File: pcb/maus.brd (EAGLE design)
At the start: 100 x 100 mm, 84 parts, among them J1 SS-52300-001, Q1 BSS123, Q2 BSS123, Q3 BSS123, Q4 BSS123, Q5 BSS123, Q6 PMN30XPEAHEATSINK, Q7 PMN30XPEAHEATSINK, U1 ESP32-S2-WROOM, U2 CH340C, U4 LP3965EMP-3.3, U5 LSM9DS1TR, U6 LM358DR

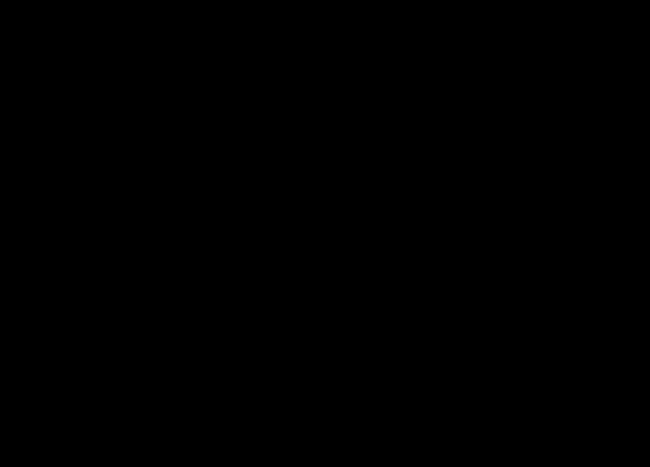
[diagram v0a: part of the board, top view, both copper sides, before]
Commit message: add: lib MBRS360
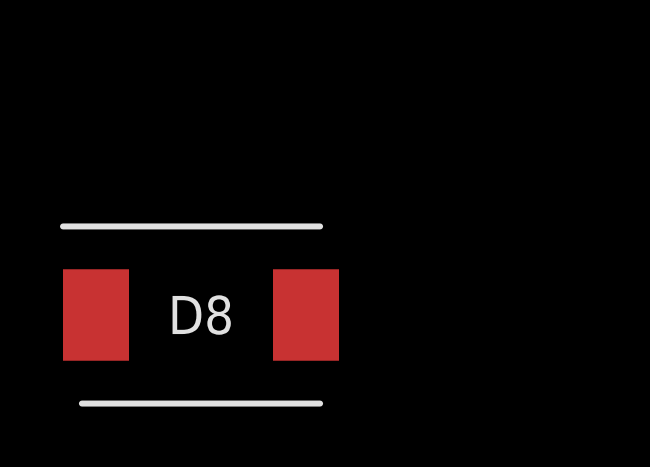
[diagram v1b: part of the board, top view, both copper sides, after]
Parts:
- added D8: VS-MBRS360-M3_9AT, shared:DIOM7959X262N

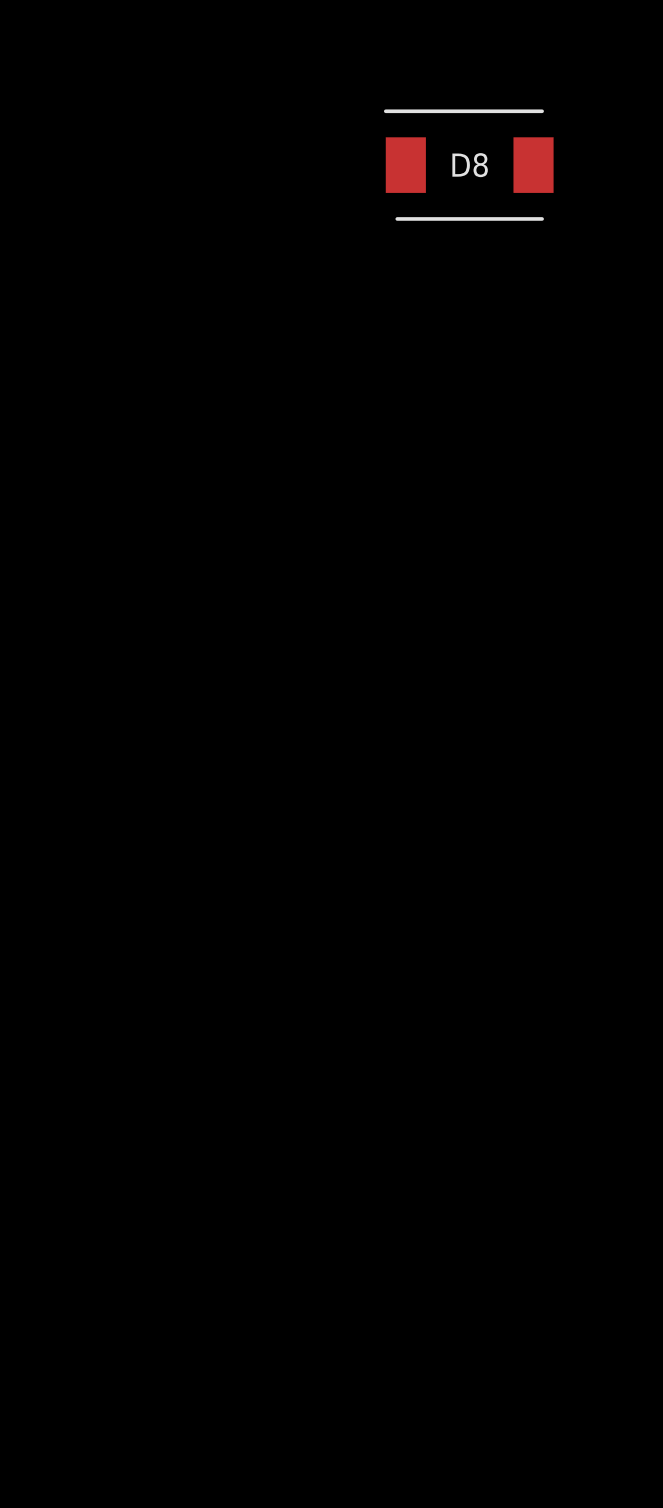
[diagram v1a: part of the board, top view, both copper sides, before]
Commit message: Added diodes for hbridge
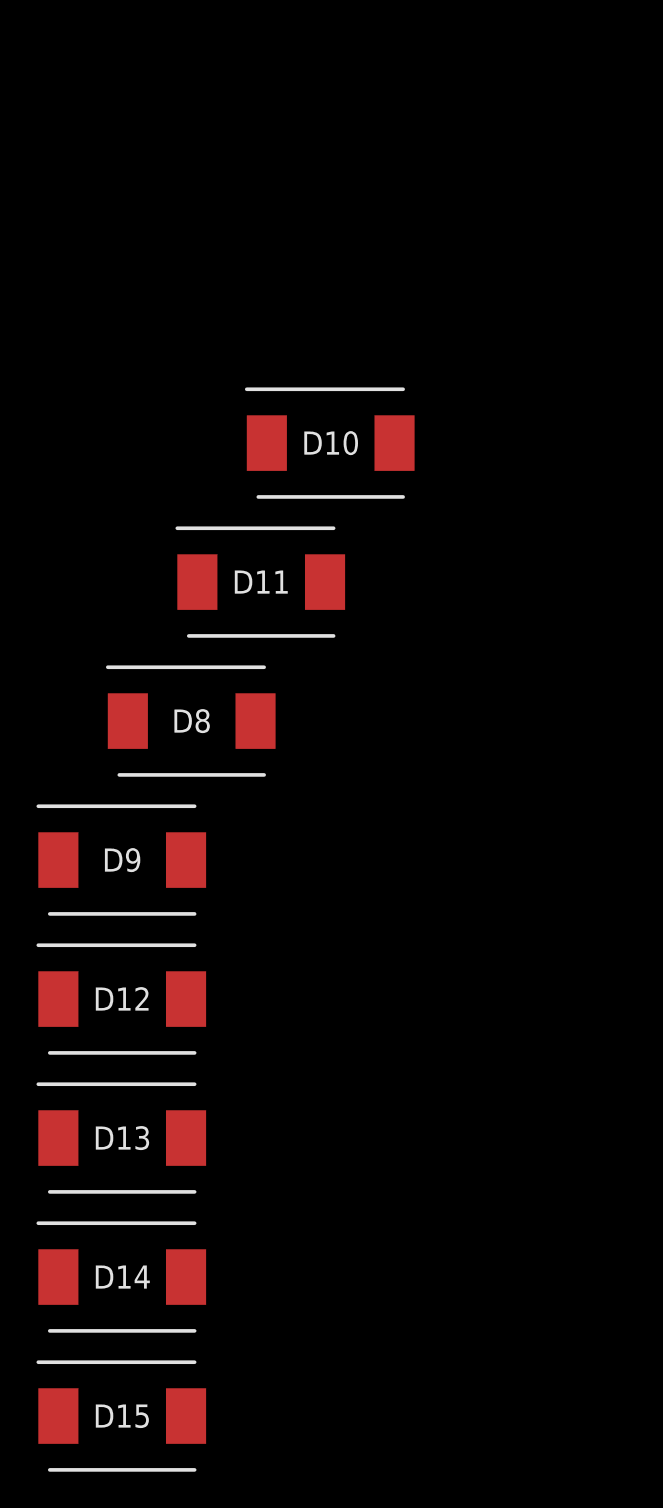
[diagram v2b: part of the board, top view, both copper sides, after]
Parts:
- added D10, D11, D12, D13, D14, D15, D9: VS-MBRS360-M3_9AT, shared:DIOM7959X262N
- moved D8 34.1 mm to (-62.2, -29.2)
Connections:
- net GND: now also D10.2, D11.2, D12.2, D13.2
- net M1_M+: now also D11.1, D8.2
- net M1_M-: now also D10.1, D9.2
- net M2_M+: now also D12.1, D15.2
- net M2_M-: now also D13.1, D14.2
- net VBAT: now also D14.1, D15.1, D8.1, D9.1

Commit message: Attached ENABLE pins to PWM
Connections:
- removed net H_EN: CR1.14, CR1.8, U1.16
- new net H_EN_A: CR1.8, U1.10
- new net H_EN_B: CR1.14, U1.16
- net IO7: no longer U1.10
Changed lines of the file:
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@@
 <wire x1="60.6044" y1="46.355" x2="72.56" y2="39.38" width="0" layer="19" extent="1-1"/>
-</signal>
-<signal name="H_EN">
-<contactref element="CR1" pad="8"/>
-<contactref element="CR1" pad="14"/>
-<contactref element="U1" pad="16"/>
-<wire x1="76.06" y1="38.63" x2="74.0156" y2="48.895" width="0" layer="19" extent="1-1"/>
-<wire x1="60.6044" y1="47.625" x2="74.0156" y2="48.895" width="0" layer="19" extent="1-1"/>
 </signal>
 <signal name="ESP32_M1_CH_A">
@@
 <signal name="IO7">
 <contactref element="JP5" pad="10"/>
-<contactref element="U1" pad="10"/>
-<wire x1="76.06" y1="29.63" x2="78.74" y2="80.01" width="0" layer="19" extent="1-1"/>
 </signal>
 <signal name="D_N">
@@
 <wire x1="58.56" y1="35.63" x2="66.24" y2="71.335" width="0" layer="19" extent="1-1"/>
 </signal>
+<signal name="H_EN_A">
+<contactref element="U1" pad="10"/>
+<contactref element="CR1" pad="8"/>
+<wire x1="76.06" y1="29.63" x2="60.6044" y2="47.625" width="0" layer="19" extent="1-1"/>
+</signal>
+<signal name="H_EN_B">
+<contactref element="U1" pad="16"/>
+<contactref element="CR1" pad="14"/>
+<wire x1="76.06" y1="38.63" x2="74.0156" y2="48.895" width="0" layer="19" extent="1-1"/>
+</signal>
 </signals>

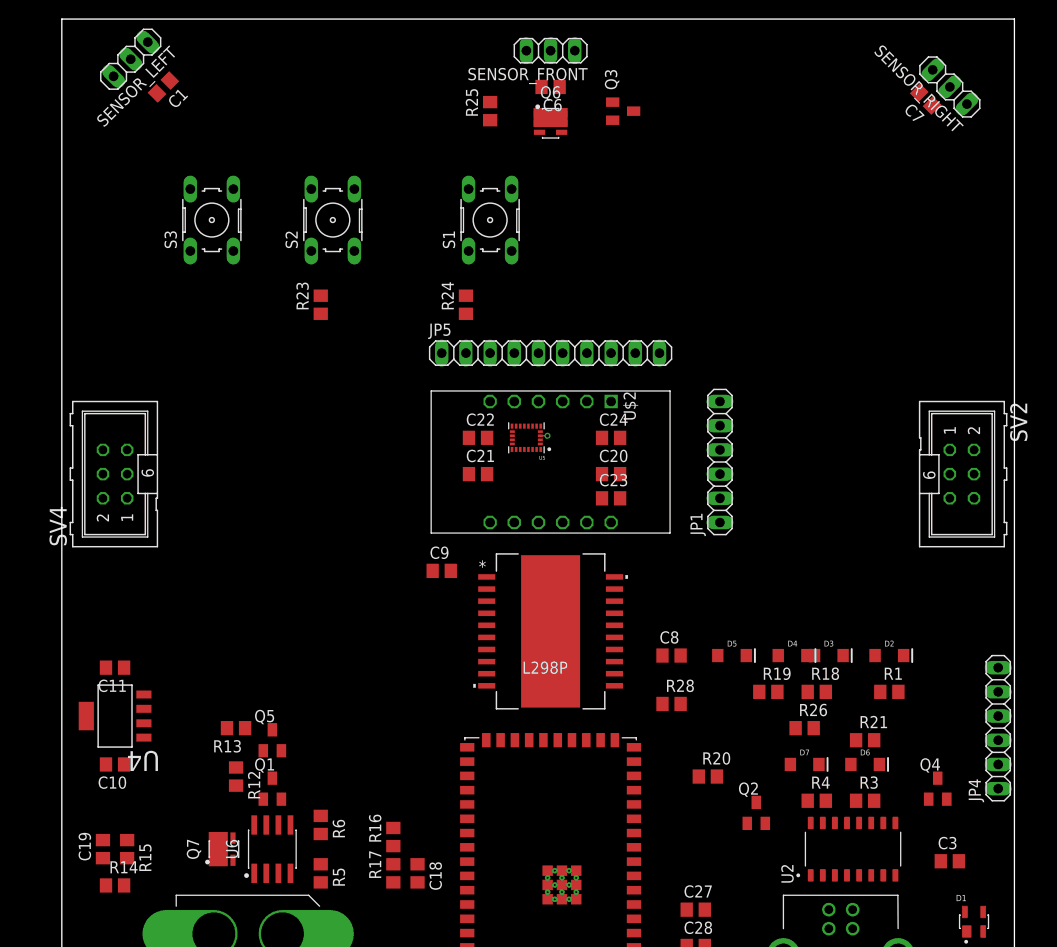
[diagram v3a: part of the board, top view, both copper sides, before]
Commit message: Halterungen in brd hinzugefügt
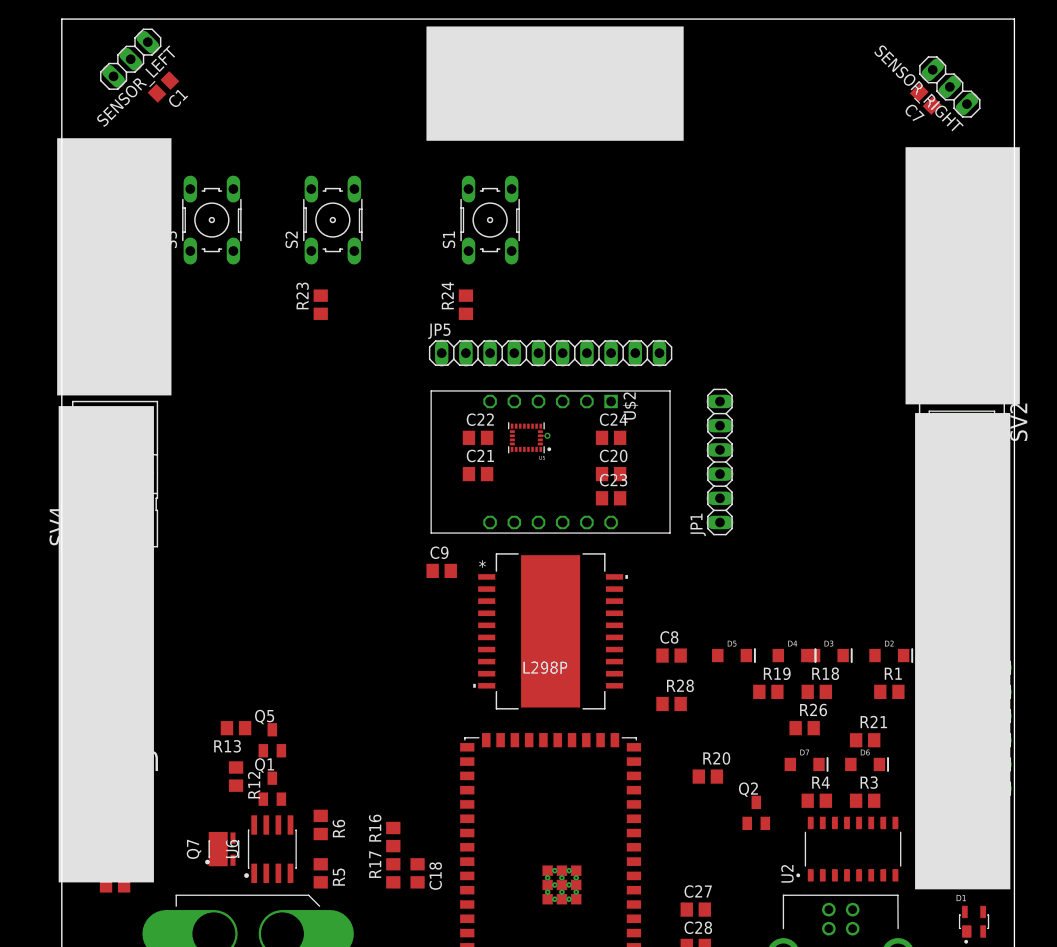
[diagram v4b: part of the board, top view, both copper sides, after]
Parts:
- added U$1, U$5: (no value), shared:MOTOR_HALTERUNG
- added U$6, U$7, U$8: (no value), shared:SENSOR_HALTERUNG

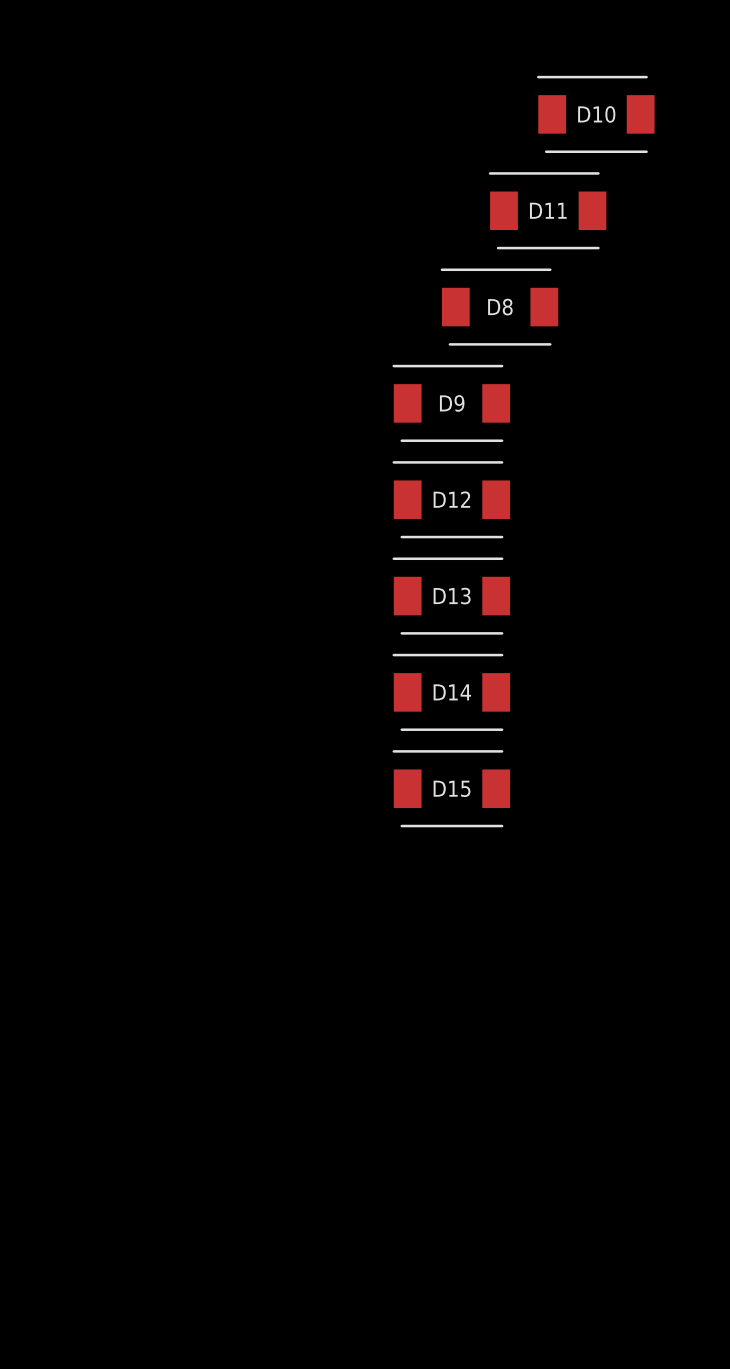
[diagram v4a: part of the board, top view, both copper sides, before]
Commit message: Changed diodes
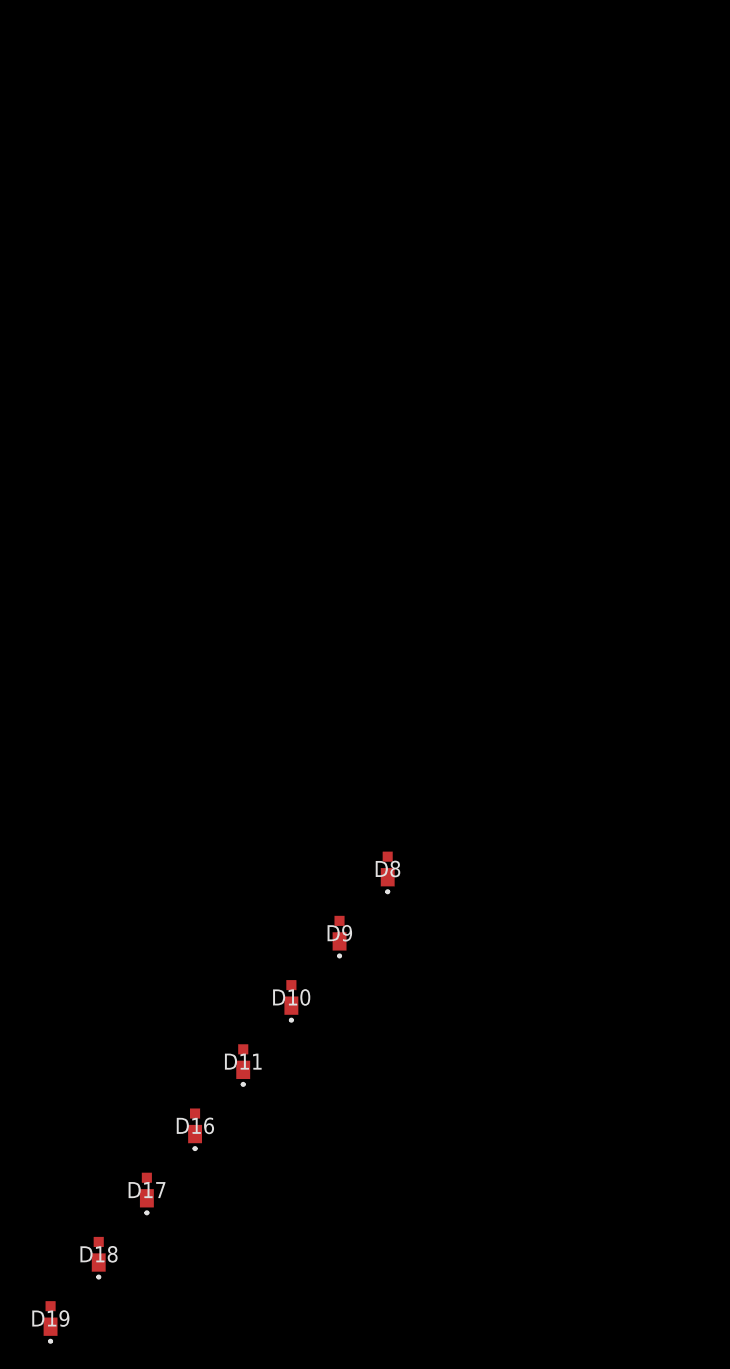
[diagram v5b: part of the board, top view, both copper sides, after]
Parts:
- removed D12, D13, D14, D15: VS-MBRS360-M3_9AT, shared:DIOM7959X262N
- added D16, D17, D18, D19: RBR2VWM40ATF, shared:RB068VWM100
- D10, D11, D8, D9: value VS-MBRS360-M3_9AT -> RBR2VWM40ATF; device shared:DIOM7959X262N -> shared:RB068VWM100
- moved D10 73.9 mm to (-78.7, -83.8)
- moved D11 71.5 mm to (-82.5, -88.9)
- moved D8 45.3 mm to (-71.1, -73.7)
- moved D9 42.8 mm to (-74.9, -78.7)
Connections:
- net GND: now also D19.2; no longer D12.2, D13.2
- net M1_M+: now also D9.2; no longer D8.2
- net M1_M-: now also D8.2; no longer D9.2
- net M2_M+: now also D16.2; no longer D12.1, D15.2
- net M2_M-: now also D17.2, D19.1; no longer D13.1, D14.2
- net VBAT: now also D16.1, D17.1; no longer D14.1, D15.1
